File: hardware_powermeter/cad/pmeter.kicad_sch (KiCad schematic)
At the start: 0 parts

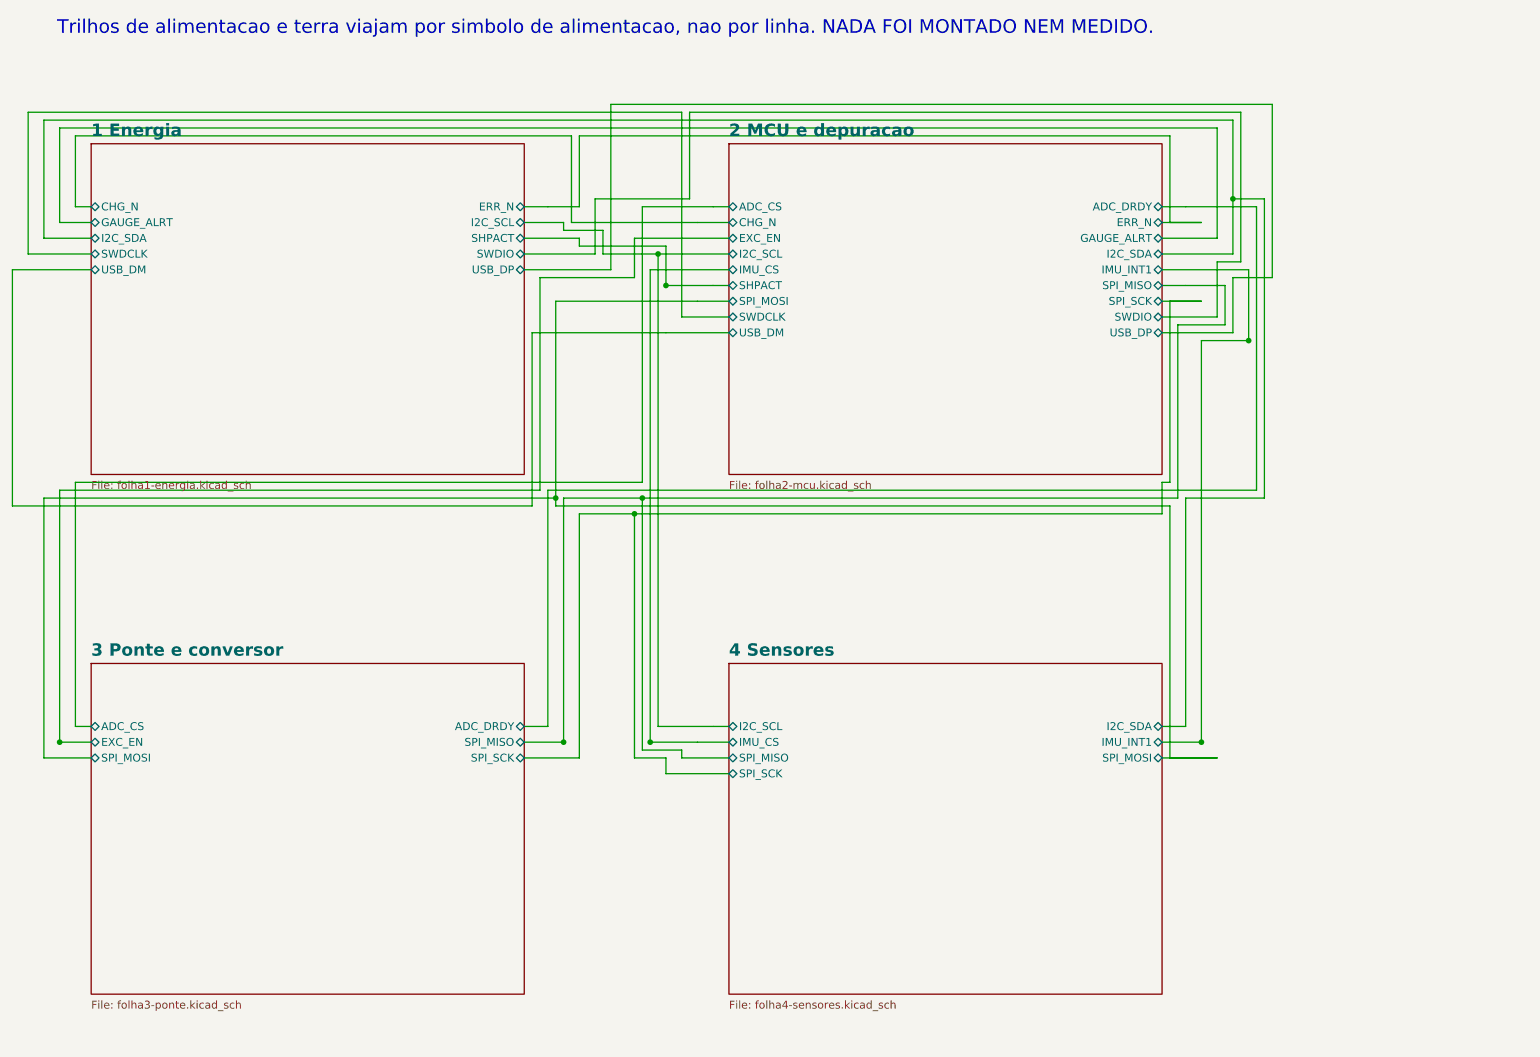
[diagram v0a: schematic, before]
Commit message: feat(hardware): draw the module for real, and bond the pod to flat metal
Two things the owner asked for, and one the second of them found.

The module gets a body instead of a box. Every DIMENSION is off the maker's
mechanical drawing - the one the footprint is generated from, which closes on
itself three independent ways - and every COLOUR is read off the product
photo, and that difference is recorded rather than smoothed over: a dimension
that closes three ways is evidence, a colour from a photograph is a reading.
It is not one box, because the part is not one box and drawing it as one
hides what decides the layout: a BLACK printed circuit (Holyiot's photo, not
the green of the ME54BS13), a shield can that reads dark rather than as
bright tin, the CERAMIC ANTENNA as an ivory block with metallised ends
sitting outside the can in the 3,80 mm band the drawing keeps clear of pads,
and the gold pads on the underside. Forty-one solids.

It is drawn 2,40 mm tall, and that is a RESERVATION, not a measurement: the
advert gives no height at all. A can over a 0,80 mm board runs 1,8 to 2,2 in
this class, so 2,40 has margin, and drawing it at the reservation makes the
body, the lid's ceiling and the new rule PD18 carry the same number - a part
that arrives taller is then caught by a rule instead of by a lid that will
not close.

The owner asked for the open questions to be measured rather than waited for,
so each one became a requirement with a rule that checks it. The crank's
numbers are the CLASS's - Shimano 105 and Ultegra, the narrow end of the
arm's taper, the tight end of road frame clearance - and PD17 measures the
pod against them. It failed on the first run, and the finding is real: the
arm's inner face is not flat across. A fillet of about 2,5 mm on each side
leaves only 15 of the class's 20 mm flat, and a 19,0 mm pod bonded across its
whole underside would sit on those radii on both sides - adhesive thick at
the edges, thin in the middle, and a joint that peels from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
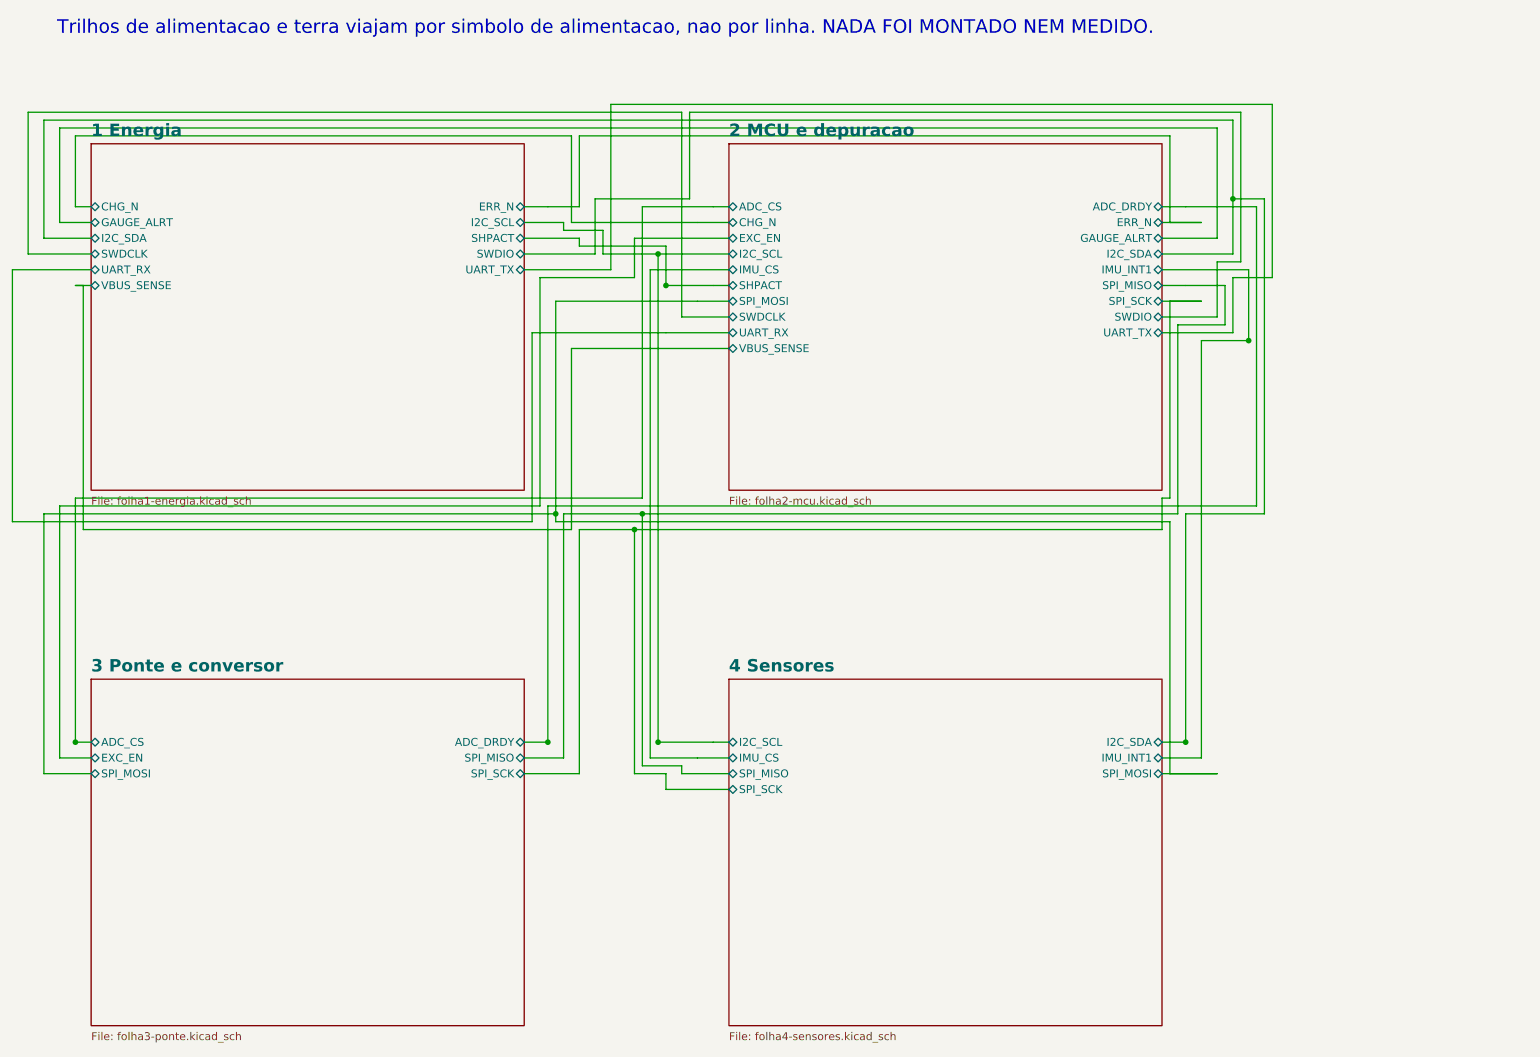
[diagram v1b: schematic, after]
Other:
- sheet 1 Energia ports: added UART_RX, UART_TX, VBUS_SENSE; removed USB_DM, USB_DP
- sheet 2 MCU e depuracao ports: added UART_RX, UART_TX, VBUS_SENSE; removed USB_DM, USB_DP
